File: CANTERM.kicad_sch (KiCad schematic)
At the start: 7 parts, among them J1 Conn_01x03_Pin, J2 Conn_01x03_Pin, SW1 SW_DIP_x01

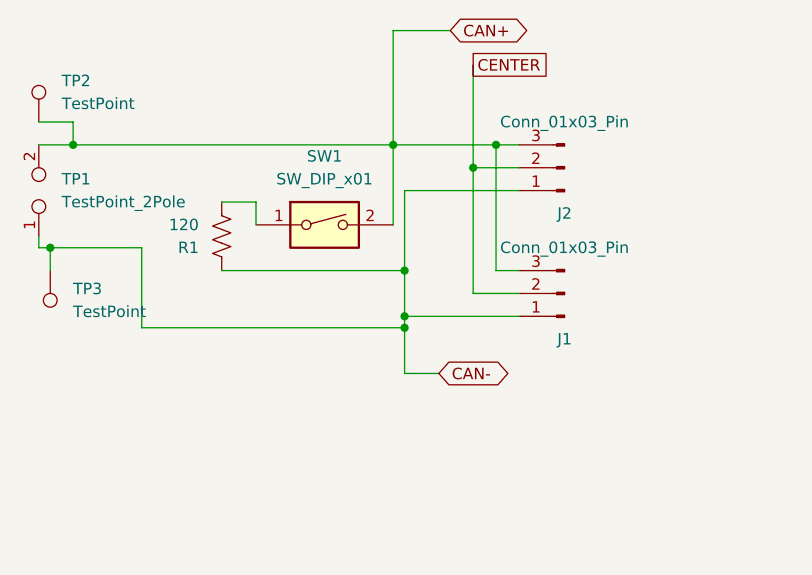
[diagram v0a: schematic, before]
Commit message: 3rd connector footprint for stub
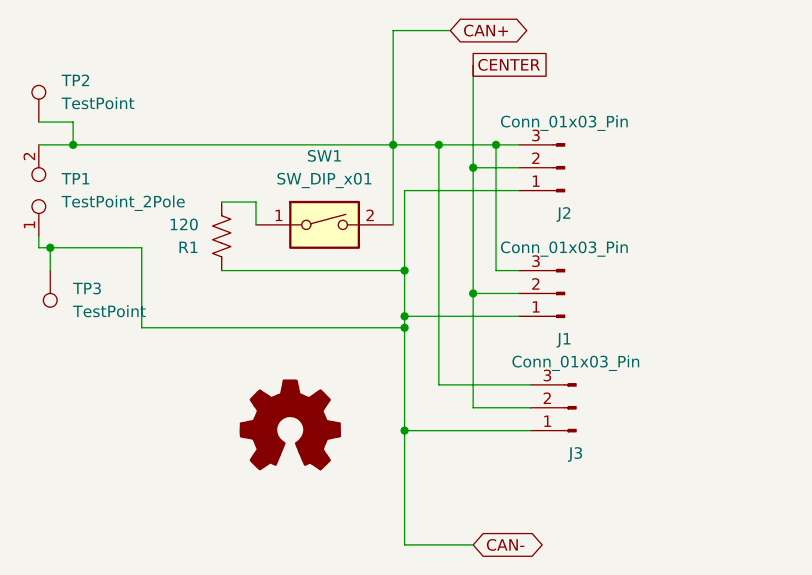
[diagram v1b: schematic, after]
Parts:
- added J3: Conn_01x03_Pin, Connector_Molex:Molex_SL_171971-0003_1x03_P2.54mm_Vertical, symbol Connector:Conn_01x03_Pin
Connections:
- net CAN+: now also J3.3 (Pin_3)
- net CAN-: now also J3.1 (Pin_1)
- net CENTER: now also J3.2 (Pin_2)
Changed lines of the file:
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@@
+	)
+	(junction
+		(at 156.21 73.66)
+		(diameter 0)
+		(color 0 0 0 0)
+	)
+	(junction
+		(at 152.4 57.15)
+		(diameter 0)
+		(color 0 0 0 0)
 	)
 	(junction
@@
 		(color 0 0 0 0)
 	)
+	(junction
+		(at 148.59 88.9)
+		(diameter 0)
+		(color 0 0 0 0)
+	)
+	(wire
+		(pts
+			(xy 152.4 83.82) (xy 162.56 83.82)
+		)
+		(stroke
+			(width 0)
+			(type default)
+		)
+	)
 	(wire
 		(pts
@@
 	(wire
 		(pts
+			(xy 152.4 83.82) (xy 152.4 57.15)
+		)
+		(stroke
+			(width 0)
+			(type default)
+		)
+	)
+	(wire
+		(pts
 			(xy 107.95 57.15) (xy 111.76 57.15)
 		)
@@
 	(wire
 		(pts
-			(xy 148.59 82.55) (xy 152.4 82.55)
+			(xy 148.59 101.6) (xy 156.21 101.6)
 		)
 		(stroke
@@
 	(wire
 		(pts
-			(xy 158.75 57.15) (xy 147.32 57.15)
+			(xy 158.75 57.15) (xy 152.4 57.15)
 		)
 		(stroke
@@
 	(wire
 		(pts
+			(xy 162.56 86.36) (xy 156.21 86.36)
+		)
+		(stroke
+			(width 0)
+			(type default)
+		)
+	)
+	(wire
+		(pts
 			(xy 156.21 59.69) (xy 156.21 73.66)
 		)
@@
 	(wire
 		(pts
+			(xy 148.59 88.9) (xy 148.59 101.6)
+		)
+		(stroke
+			(width 0)
+			(type default)
+		)
+	)
+	(wire
+		(pts
+			(xy 148.59 88.9) (xy 162.56 88.9)
+		)
+		(stroke
+			(width 0)
+			(type default)
+		)
+	)
+	(wire
+		(pts
+			(xy 152.4 57.15) (xy 147.32 57.15)
+		)
+		(stroke
+			(width 0)
+			(type default)
+		)
+	)
+	(wire
+		(pts
 			(xy 158.75 57.15) (xy 161.29 57.15)
 		)
@@
 	(wire
 		(pts
-			(xy 148.59 77.47) (xy 148.59 82.55)
+			(xy 156.21 86.36) (xy 156.21 73.66)
+		)
+		(stroke
+			(width 0)
+			(type default)
+		)
+	)
+	(wire
+		(pts
+			(xy 148.59 77.47) (xy 148.59 88.9)
 		)
 		(stroke
@@
 	(global_label "CAN-"
 		(shape bidirectional)
-		(at 152.4 82.55 0)
+		(at 156.21 101.6 0)
 		(fields_autoplaced yes)
 		(effects
@@
 		)
 		(property "Intersheetrefs" "${INTERSHEET_REFS}"
-			(at 161.758 82.55 0)
+			(at 165.568 101.6 0)
 			(effects
 				(font
@@
 	)
 	(symbol
+		(lib_id "Connector:Conn_01x03_Pin")
+		(at 167.64 86.36 180)
+		(unit 1)
+		(exclude_from_sim no)
+		(in_bom yes)
+		(on_board yes)
+		(dnp no)
+		(property "Reference" "J3"
+			(at 167.64 91.44 0)
+			(effects
+				(font
+					(size 1.27 1.27)
+				)
+			)
+		)
+		(property "Value" "Conn_01x03_Pin"
+			(at 167.64 81.28 0)
+			(effects
+				(font
+					(size 1.27 1.27)
+				)
+			)
+		)
+		(property "Footprint" "Connector_Molex:Molex_SL_171971-0003_1x03_P2.54mm_Vertical"
+			(at 167.64 86.36 0)
+			(effects
+				(font
+					(size 1.27 1.27)
+				)
+				(hide yes)
+			)
+		)
+		(property "Datasheet" "~"
+			(at 167.64 86.36 0)
+			(effects
+				(font
+					(size 1.27 1.27)
+				)
+				(hide yes)
+			)
+		)
+		(property "Description" "Generic connector, single row, 01x03, script generated"
+			(at 167.64 86.36 0)
+			(effects
+				(font
+					(size 1.27 1.27)
+				)
+				(hide yes)
+			)
+		)
+		(pin "2"
+		)
+		(pin "1"
+		)
+		(pin "3"
+		)
+		(instances
+			(project "CANTERM"
+				(path "/9c34a7b5-eb60-481f-a74c-631ac911a0f2"
+					(reference "J3")
+					(unit 1)
+				)
+			)
+		)
+	)
+	(symbol
 		(lib_id "Device:R_US")
 		(at 128.27 67.31 180)
@@
 					(unit 1)
 				)
+			)
+		)
+	)
+	(symbol
+		(lib_id "Graphic:Logo_Open_Hardware_Small")
+		(at 135.89 88.9 0)
+		(unit 1)
+		(exclude_from_sim no)
+		(in_bom no)
+		(on_board no)
+		(dnp no)
+		(fields_autoplaced yes)
+		(property "Reference" "#SYM1"
+			(at 135.89 81.915 0)
+			(effects
+				(font
+					(size 1.27 1.27)
+				)
+				(hide yes)
+			)
+		)
+		(property "Value" "Logo_Open_Hardware_Small"
+			(at 135.89 94.615 0)
+			(effects
+				(font
+					(size 1.27 1.27)
+				)
+				(hide yes)
+			)
+		)
+		(property "Footprint" ""
+			(at 135.89 88.9 0)
+			(effects
+				(font
+					(size 1.27 1.27)
+				)
+				(hide yes)
+			)
+		)
+		(property "Datasheet" "~"
+			(at 135.89 88.9 0)
+			(effects
+				(font
+					(size 1.27 1.27)
+				)
+				(hide yes)
+			)
+		)
+		(property "Description" "Open Hardware logo, small"
+			(at 135.89 88.9 0)
+			(effects
+				(font
+					(size 1.27 1.27)
+				)
+				(hide yes)
+			)
+		)
+		(property "Sim.Enable" "0"
+			(at 135.89 88.9 0)
+			(effects
+				(font
+					(size 1.27 1.27)
+				)
+				(hide yes)
+			)
+		)
+		(instances
+			(project ""
+				(path "/9c34a7b5-eb60-481f-a74c-631ac911a0f2"
+					(reference "#SYM1")
+					(unit 1)
+				)

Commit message: crying, correctly labeled pins
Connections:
- net CAN+: now also J1.1 (Pin_1), J2.1 (Pin_1), J3.1 (Pin_1), R1.1, TP1.1, TP3.1; no longer J1.3 (Pin_3), J2.3 (Pin_3), J3.3 (Pin_3), SW1.2, TP1.2, TP2.1
- net CAN-: now also J1.3 (Pin_3), J2.3 (Pin_3), J3.3 (Pin_3), SW1.2, TP1.2, TP2.1; no longer J1.1 (Pin_1), J2.1 (Pin_1), J3.1 (Pin_1), R1.1, TP1.1, TP3.1
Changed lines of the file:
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@@
+	)
+	(junction
+		(at 162.56 83.82)
+		(diameter 0)
+		(color 0 0 0 0)
 	)
 	(junction
@@
 	)
 	(junction
-		(at 148.59 88.9)
+		(at 162.56 88.9)
 		(diameter 0)
 		(color 0 0 0 0)
@@
 	(wire
 		(pts
+			(xy 162.56 88.9) (xy 182.88 88.9)
+		)
+		(stroke
+			(width 0)
+			(type default)
+		)
+	)
+	(wire
+		(pts
 			(xy 152.4 83.82) (xy 162.56 83.82)
 		)
@@
 	(wire
 		(pts
-			(xy 148.59 101.6) (xy 156.21 101.6)
-		)
-		(stroke
-			(width 0)
-			(type default)
-		)
-	)
-	(wire
-		(pts
 			(xy 148.59 62.23) (xy 148.59 71.12)
 		)
@@
 	(wire
 		(pts
-			(xy 147.32 44.45) (xy 153.67 44.45)
-		)
-		(stroke
-			(width 0)
-			(type default)
-		)
-	)
-	(wire
-		(pts
 			(xy 148.59 71.12) (xy 128.27 71.12)
 		)
@@
 	(wire
 		(pts
-			(xy 148.59 88.9) (xy 148.59 101.6)
+			(xy 162.56 83.82) (xy 182.88 83.82)
 		)
 		(stroke
@@
 		(pts
 			(xy 156.21 48.26) (xy 156.21 59.69)
-		)
-		(stroke
-			(width 0)
-			(type default)
-		)
-	)
-	(wire
-		(pts
-			(xy 147.32 44.45) (xy 147.32 57.15)
 		)
 		(stroke
@@
 	(global_label "CAN-"
 		(shape bidirectional)
-		(at 156.21 101.6 0)
+		(at 182.88 83.82 0)
 		(fields_autoplaced yes)
 		(effects
@@
 		)
 		(property "Intersheetrefs" "${INTERSHEET_REFS}"
-			(at 165.568 101.6 0)
+			(at 192.238 83.82 0)
 			(effects
 				(font
@@
 	(global_label "CAN+"
 		(shape bidirectional)
-		(at 153.67 44.45 0)
+		(at 182.88 88.9 0)
 		(fields_autoplaced yes)
 		(effects
@@
 		)
 		(property "Intersheetrefs" "${INTERSHEET_REFS}"
-			(at 163.028 44.45 0)
+			(at 192.238 88.9 0)
 			(effects
 				(font
@@
 		(at 135.89 88.9 0)
 		(unit 1)
-		(exclude_from_sim no)
+		(exclude_from_sim yes)
 		(in_bom no)
 		(on_board no)
@@
 			(at 135.89 88.9 0)
 			(effects
-				(font
-					(size 1.27 1.27)
-				)
-				(hide yes)
-			)
-		)
-		(property "Sim.Enable" "0"
-			(at 135.89 88.9 0)
-			(effects
